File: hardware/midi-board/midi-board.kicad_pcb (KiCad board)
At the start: 2 copper layers, 88 x 45 mm, 41 parts, among them J1 MIDI OUT, J10 Conn_02x02_Odd_Even, J2 MIDI IN, J3 Qwiic, J4 A0, J5 A1, J6 Qwiic, J7 UART, J8 I2C, U1 74LVC1G07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

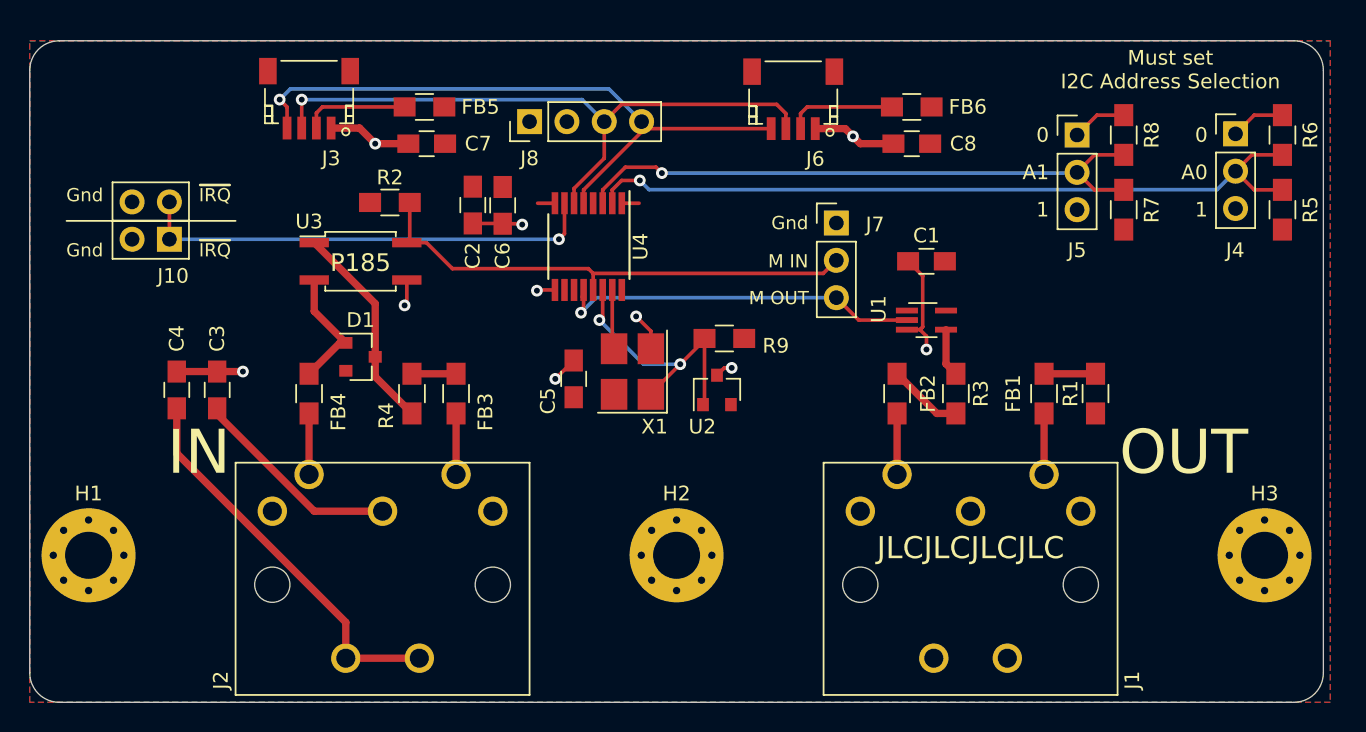
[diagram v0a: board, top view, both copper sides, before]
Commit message: Made most changes for rev 2 of MIDI board
* Silkscreen for I2C header
* Converted from specialized I2C UART to an STM32G0
* Replace the specialized 74-series open-drain buffer with a BJT
* Switch to using a BJT to pull down the interrupt line.
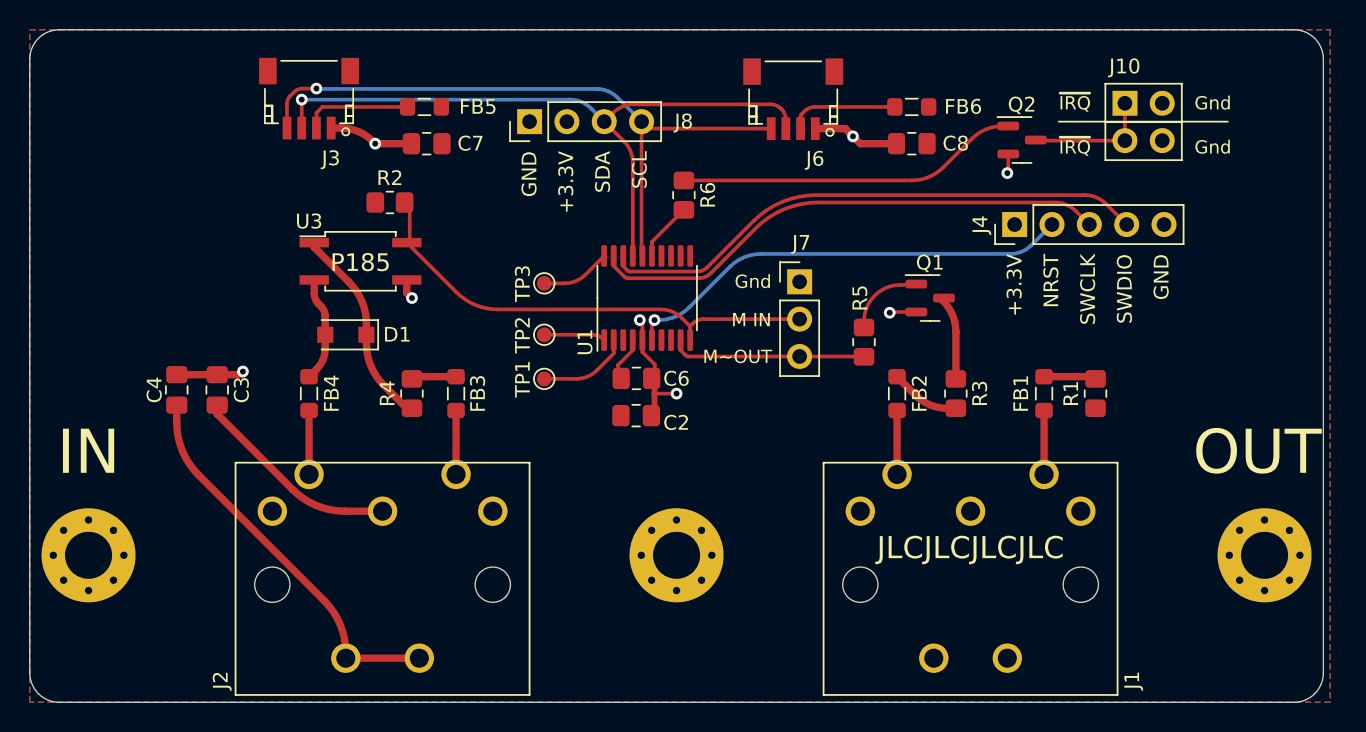
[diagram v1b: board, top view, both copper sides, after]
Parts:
- removed C1, C5: 0.1uF, Capacitors_SMD:C_0805_HandSoldering
- removed J5: A1, Pin_Headers:Pin_Header_Straight_1x03_Pitch2.54mm
- removed R7, R8: DNP, Resistors_SMD:R_0805_HandSoldering
- removed R9: 0/DNP, Resistors_SMD:R_0805_HandSoldering
- removed U2: MCP1X0-315, TO_SOT_Packages_SMD:SOT-23
- removed U4: SC16IS740, Housings_SSOP:TSSOP-16_4.4x5mm_Pitch0.65mm
- removed X1: SG-5032CAN, Oscillators:Oscillator_SMD_SeikoEpson_SG8002CE-4pin_3.2x2.5mm_HandSoldering
- added Q1: Q_NPN_BEC, Package_TO_SOT_SMD:SOT-23, F.Cu at (177.2, 52.5)
- added Q2: Q_NPN_BEC, Package_TO_SOT_SMD:SOT-23, F.Cu at (183.5, 41.8)
- added TP1: TestPoint, TestPoint:TestPoint_Pad_D1.0mm, F.Cu at (151.0, 58.0)
- added TP2: TestPoint, TestPoint:TestPoint_Pad_D1.0mm, F.Cu at (151.0, 55.0)
- added TP3: TestPoint, TestPoint:TestPoint_Pad_D1.0mm, F.Cu at (151.0, 51.5)
- C2, C3, C4, C6, C7, C8: footprint Capacitors_SMD:C_0805_HandSoldering -> Capacitor_SMD:C_0805_2012Metric_Pad1.18x1.45mm_HandSolder
- D1: value BAS16 -> Vf>=4; footprint Diodes_SMD:D_SOT-23_ANK -> Diode_SMD:D_SOD-123F
- FB1, FB2, FB3, FB4, FB5, FB6: footprint Inductors_SMD:L_0805_HandSoldering -> Inductor_SMD:L_0805_2012Metric_Pad1.05x1.20mm_HandSolder
- J4: value A0 -> Serial Wire; footprint Pin_Headers:Pin_Header_Straight_1x03_Pitch2.54mm -> Connector_PinHeader_2.54mm:PinHeader_1x05_P2.54mm_Vertical
- R1, R2, R3, R4: footprint Resistors_SMD:R_0805_HandSoldering -> Resistor_SMD:R_0805_2012Metric_Pad1.20x1.40mm_HandSolder
- R5, R6: value DNP -> 10k; footprint Resistors_SMD:R_0805_HandSoldering -> Resistor_SMD:R_0805_2012Metric_Pad1.20x1.40mm_HandSolder
- U1: value 74LVC1G07 -> STM32G030Fx; footprint TO_SOT_Packages_SMD:SOT-353_SC-70-5_Handsoldering -> Package_SO:TSSOP-20_4.4x6.5mm_P0.65mm
- moved J10 65.7 mm to (190.5, 39.2), turned to 0 degrees
- moved R6 40.9 mm to (160.5, 45.5)
- moved R5 29.9 mm to (172.8, 55.5)
- moved U1 19.1 mm to (158.0, 52.5), turned to 90 degrees
- moved C2 18.1 mm to (157.2, 60.5), turned to 180 degrees
- moved J4 16.2 mm to (183.0, 47.5), turned to 90 degrees
- moved C6 14.9 mm to (157.3, 58.0), turned to 180 degrees
- moved J7 4.72 mm to (168.4, 51.4)
- moved D1 1.80 mm to (137.5, 55.0), turned to 180 degrees
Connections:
- net /~IRQ renamed Net-(J10-Pad1)
- J1 pad 1: (no net) -> unconnected-(J1-Pad1)
- J1 pad 3: (no net) -> unconnected-(J1-Pad3)
- J2 pad 1: (no net) -> unconnected-(J2-Pad1)
- J2 pad 3: (no net) -> unconnected-(J2-Pad3)
- J4 pad 1: GND -> +3V3
- J4 pad 2: /A0 -> /NRST
- J4 pad 3: +3V3 -> /SWCLK
- J7 pad 3: /TX -> /~{TX}
- R5 pad 1: +3V3 -> /~{TX}
- R5 pad 2: /A0 -> Net-(Q1-Pad1)
- R6 pad 1: GND -> Net-(Q2-Pad1)
- R6 pad 2: /A0 -> /IRQ
- U1 pad 1: (no net) -> Net-(TP2-Pad1)
- U1 pad 2: /TX -> Net-(TP1-Pad1)
- U1 pad 3: GND -> unconnected-(U1-Pad3)
- U1 pad 4: Net-(R3-Pad1) -> +3V3
- U1 pad 5: +3V3 -> GND
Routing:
- net /A0: track 51.7 -> 0.00 mm, vias 1 -> 0
- net /A1: track 41.3 -> 0.00 mm, vias 1 -> 0
- net /SWDIO: track 0.00 -> 37.6 mm
- net /SWCLK: track 0.00 -> 35.7 mm
- net /NRST: track 0.00 -> 30.8 mm, vias 0 -> 1
- net /TX: track 25.0 -> 0.00 mm, vias 1 -> 0
- net Net-(Q2-Pad1): track 0.00 -> 23.3 mm
- net Net-(J10-Pad1): track 31.6 -> 8.62 mm, vias 1 -> 0
- net /~RST: track 19.0 -> 0.00 mm, vias 2 -> 0
- net GND: track 43.3 -> 28.1 mm, vias 10 -> 8
- net /~{TX}: track 0.00 -> 13.3 mm
- net Net-(TP1-Pad1): track 0.00 -> 6.26 mm
- net Net-(Q1-Pad1): track 0.00 -> 5.24 mm
- net Net-(TP3-Pad1): track 0.00 -> 4.75 mm
- net Net-(TP2-Pad1): track 0.00 -> 4.18 mm
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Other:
- board size 88 x 45 mm -> 88 x 45.8 mm
- net class Default removed
- board text added: "+3.3V"
- board text added: "GND"
- board text added: "I²C↔MIDI Rev2α http://github.com/jkominek/piano-conversion"
- board text added: "M~OUT"
- board text added: "NRST"
- board text added: "SCL"
- board text added: "SDA"
- board text added: "SWCLK"
- board text added: "SWDIO"
- board text added: "~{IRQ}"
- board text removed: "0"
- board text removed: "1"
- board text removed: "A0"
- board text removed: "A1"
- board text removed: "I²C↔MIDI Rev1 http://github.com/jkominek/piano-conversion"
- board text removed: "M OUT"
- board text removed: "Must set I2C Address Selection"
- board text removed: "~IRQ"

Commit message: Convert all other mounting holes to non-pad variety.
Reroute a few traces to be shorter.
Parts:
- H1, H2, H3: footprint Mounting_Holes:MountingHole_3.2mm_M3_Pad_Via -> MountingHole:MountingHole_3.2mm_M3
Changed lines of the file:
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@@
   (net 36 "Net-(TP2-Pad1)")
   (net 37 "Net-(TP3-Pad1)")
-  (net 38 "Net-(R3-Pad1)")
+  (net 38 "Net-(Q1-Pad3)")
   (net 39 "Net-(J10-Pad1)")
   (net 40 "Net-(Q2-Pad1)")
@@
     (fp_line (start 1 0.625) (end -1 0.625) (layer "F.Fab") (width 0.1))
     (pad "1" smd roundrect (at -1 0 270) (size 1.2 1.4) (layers "F.Cu" "F.Paste" "F.Mask") (roundrect_rratio 0.208333)
-      (net 38 "Net-(R3-Pad1)") (pintype "passive"))
+      (net 38 "Net-(Q1-Pad3)") (pintype "passive"))
     (pad "2" smd roundrect (at 1 0 270) (size 1.2 1.4) (layers "F.Cu" "F.Paste" "F.Mask") (roundrect_rratio 0.208333)
       (net 9 "Net-(FB2-Pad1)") (pintype "passive"))
@@
     )
   )
-  (footprint "Mounting_Holes:MountingHole_3.2mm_M3_Pad_Via" (layer "F.Cu")
+  (footprint "MountingHole:MountingHole_3.2mm_M3" (layer "F.Cu")
     (at 120 70)
-    (descr "Mounting Hole 3.2mm, M3")
-    (tags "mounting hole 3.2mm m3")
+    (descr "Mounting Hole 3.2mm, no annular, M3")
+    (tags "mounting hole 3.2mm no annular m3")
     (property "Sheetfile" "midi-board.kicad_sch")
     (property "Sheetname" "")
@@
     (fp_circle (center 0 0) (end 3.2 0) (layer "Cmts.User") (width 0.15) (fill none))
     (fp_circle (center 0 0) (end 3.45 0) (layer "F.CrtYd") (width 0.05) (fill none))
-    (pad "1" thru_hole circle locked (at 1.697056 -1.697056) (size 0.8 0.8) (drill 0.5) (layers *.Cu *.Mask))
-    (pad "1" thru_hole circle locked (at 0 0) (size 6.4 6.4) (drill 3.2) (layers *.Cu *.Mask))
-    (pad "1" thru_hole circle locked (at 0 -2.4) (size 0.8 0.8) (drill 0.5) (layers *.Cu *.Mask))
-    (pad "1" thru_hole circle locked (at -2.4 0) (size 0.8 0.8) (drill 0.5) (layers *.Cu *.Mask))
-    (pad "1" thru_hole circle locked (at 1.697056 1.697056) (size 0.8 0.8) (drill 0.5) (layers *.Cu *.Mask))
-    (pad "1" thru_hole circle locked (at 0 2.4) (size 0.8 0.8) (drill 0.5) (layers *.Cu *.Mask))
-    (pad "1" thru_hole circle locked (at -1.697056 1.697056) (size 0.8 0.8) (drill 0.5) (layers *.Cu *.Mask))
-    (pad "1" thru_hole circle locked (at 2.4 0) (size 0.8 0.8) (drill 0.5) (layers *.Cu *.Mask))
-    (pad "1" thru_hole circle locked (at -1.697056 -1.697056) (size 0.8 0.8) (drill 0.5) (layers *.Cu *.Mask))
-  )
-  (footprint "Mounting_Holes:MountingHole_3.2mm_M3_Pad_Via" (layer "F.Cu")
+    (pad "" np_thru_hole circle locked (at 0 0) (size 3.2 3.2) (drill 3.2) (layers *.Cu *.Mask))
+  )
+  (footprint "MountingHole:MountingHole_3.2mm_M3" (layer "F.Cu")
     (at 160 70)
-    (descr "Mounting Hole 3.2mm, M3")
-    (tags "mounting hole 3.2mm m3")
+    (descr "Mounting Hole 3.2mm, no annular, M3")
+    (tags "mounting hole 3.2mm no annular m3")
     (property "Sheetfile" "midi-board.kicad_sch")
     (property "Sheetname" "")
@@
     (fp_circle (center 0 0) (end 3.2 0) (layer "Cmts.User") (width 0.15) (fill none))
     (fp_circle (center 0 0) (end 3.45 0) (layer "F.CrtYd") (width 0.05) (fill none))
-    (pad "1" thru_hole circle locked (at -1.697056 1.697056) (size 0.8 0.8) (drill 0.5) (layers *.Cu *.Mask))
-    (pad "1" thru_hole circle locked (at 1.697056 -1.697056) (size 0.8 0.8) (drill 0.5) (layers *.Cu *.Mask))
-    (pad "1" thru_hole circle locked (at 0 -2.4) (size 0.8 0.8) (drill 0.5) (layers *.Cu *.Mask))
-    (pad "1" thru_hole circle locked (at 0 0) (size 6.4 6.4) (drill 3.2) (layers *.Cu *.Mask))
-    (pad "1" thru_hole circle locked (at 1.697056 1.697056) (size 0.8 0.8) (drill 0.5) (layers *.Cu *.Mask))
-    (pad "1" thru_hole circle locked (at 2.4 0) (size 0.8 0.8) (drill 0.5) (layers *.Cu *.Mask))
-    (pad "1" thru_hole circle locked (at -2.4 0) (size 0.8 0.8) (drill 0.5) (layers *.Cu *.Mask))
-    (pad "1" thru_hole circle locked (at 0 2.4) (size 0.8 0.8) (drill 0.5) (layers *.Cu *.Mask))
-    (pad "1" thru_hole circle locked (at -1.697056 -1.697056) (size 0.8 0.8) (drill 0.5) (layers *.Cu *.Mask))
-  )
-  (footprint "Mounting_Holes:MountingHole_3.2mm_M3_Pad_Via" (layer "F.Cu")
+    (pad "" np_thru_hole circle locked (at 0 0) (size 3.2 3.2) (drill 3.2) (layers *.Cu *.Mask))
+  )
+  (footprint "MountingHole:MountingHole_3.2mm_M3" (layer "F.Cu")
     (at 200 70)
-    (descr "Mounting Hole 3.2mm, M3")
-    (tags "mounting hole 3.2mm m3")
+    (descr "Mounting Hole 3.2mm, no annular, M3")
+    (tags "mounting hole 3.2mm no annular m3")
     (property "Sheetfile" "midi-board.kicad_sch")
     (property "Sheetname" "")
@@
     (fp_circle (center 0 0) (end 3.2 0) (layer "Cmts.User") (width 0.15) (fill none))
     (fp_circle (center 0 0) (end 3.45 0) (layer "F.CrtYd") (width 0.05) (fill none))
-    (pad "1" thru_hole circle locked (at -2.4 0) (size 0.8 0.8) (drill 0.5) (layers *.Cu *.Mask))
-    (pad "1" thru_hole circle locked (at 0 0) (size 6.4 6.4) (drill 3.2) (layers *.Cu *.Mask))
-    (pad "1" thru_hole circle locked (at 0 -2.4) (size 0.8 0.8) (drill 0.5) (layers *.Cu *.Mask))
-    (pad "1" thru_hole circle locked (at 1.697056 1.697056) (size 0.8 0.8) (drill 0.5) (layers *.Cu *.Mask))
-    (pad "1" thru_hole circle locked (at 1.697056 -1.697056) (size 0.8 0.8) (drill 0.5) (layers *.Cu *.Mask))
-    (pad "1" thru_hole circle locked (at -1.697056 1.697056) (size 0.8 0.8) (drill 0.5) (layers *.Cu *.Mask))
-    (pad "1" thru_hole circle locked (at -1.697056 -1.697056) (size 0.8 0.8) (drill 0.5) (layers *.Cu *.Mask))
-    (pad "1" thru_hole circle locked (at 2.4 0) (size 0.8 0.8) (drill 0.5) (layers *.Cu *.Mask))
-    (pad "1" thru_hole circle locked (at 0 2.4) (size 0.8 0.8) (drill 0.5) (layers *.Cu *.Mask))
+    (pad "" np_thru_hole circle locked (at 0 0) (size 3.2 3.2) (drill 3.2) (layers *.Cu *.Mask))
   )
   (footprint "Pin_Headers:Pin_Header_Straight_1x04_Pitch2.54mm" (layer "F.Cu")
@@
       (net 1 "GND") (pinfunction "E") (pintype "passive"))
     (pad "3" smd roundrect locked (at 0.9375 0) (size 1.475 0.6) (layers "F.Cu" "F.Paste" "F.Mask") (roundrect_rratio 0.25)
-      (net 38 "Net-(R3-Pad1)") (pinfunction "C") (pintype "passive"))
+      (net 38 "Net-(Q1-Pad3)") (pinfunction "C") (pintype "passive"))
     (model "${KICAD6_3DMODEL_DIR}/Package_TO_SOT_SMD.3dshapes/SOT-23.wrl"
       (offset (xyz 0 0 0))

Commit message: Next revs of the important boards
Includes some tiny DRC tweaks for the LED power board.
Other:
- board text added: "I²C↔MIDI Rev2 http://github.com/jkominek/piano-conversion"
- board text removed: "I²C↔MIDI Rev2α http://github.com/jkominek/piano-conversion"
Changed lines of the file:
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@@
   (gr_line (start 118 80) (end 202 80) (layer "Edge.Cuts") (width 0.05))
   (gr_arc (start 202 34.25) (mid 203.414214 34.835786) (end 204 36.25) (layer "Edge.Cuts") (width 0.05))
-  (gr_text "I²C↔MIDI Rev2α\nhttp://github.com/jkominek/piano-conversion" (at 134.5 37.5 180) (layer "B.SilkS")
+  (gr_text "I²C↔MIDI Rev2\nhttp://github.com/jkominek/piano-conversion" (at 134.5 37.5 180) (layer "B.SilkS")
     (effects (font (size 1 1) (thickness 0.15)) (justify mirror))
   )
